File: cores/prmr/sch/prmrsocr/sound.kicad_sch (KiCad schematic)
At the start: 13 parts

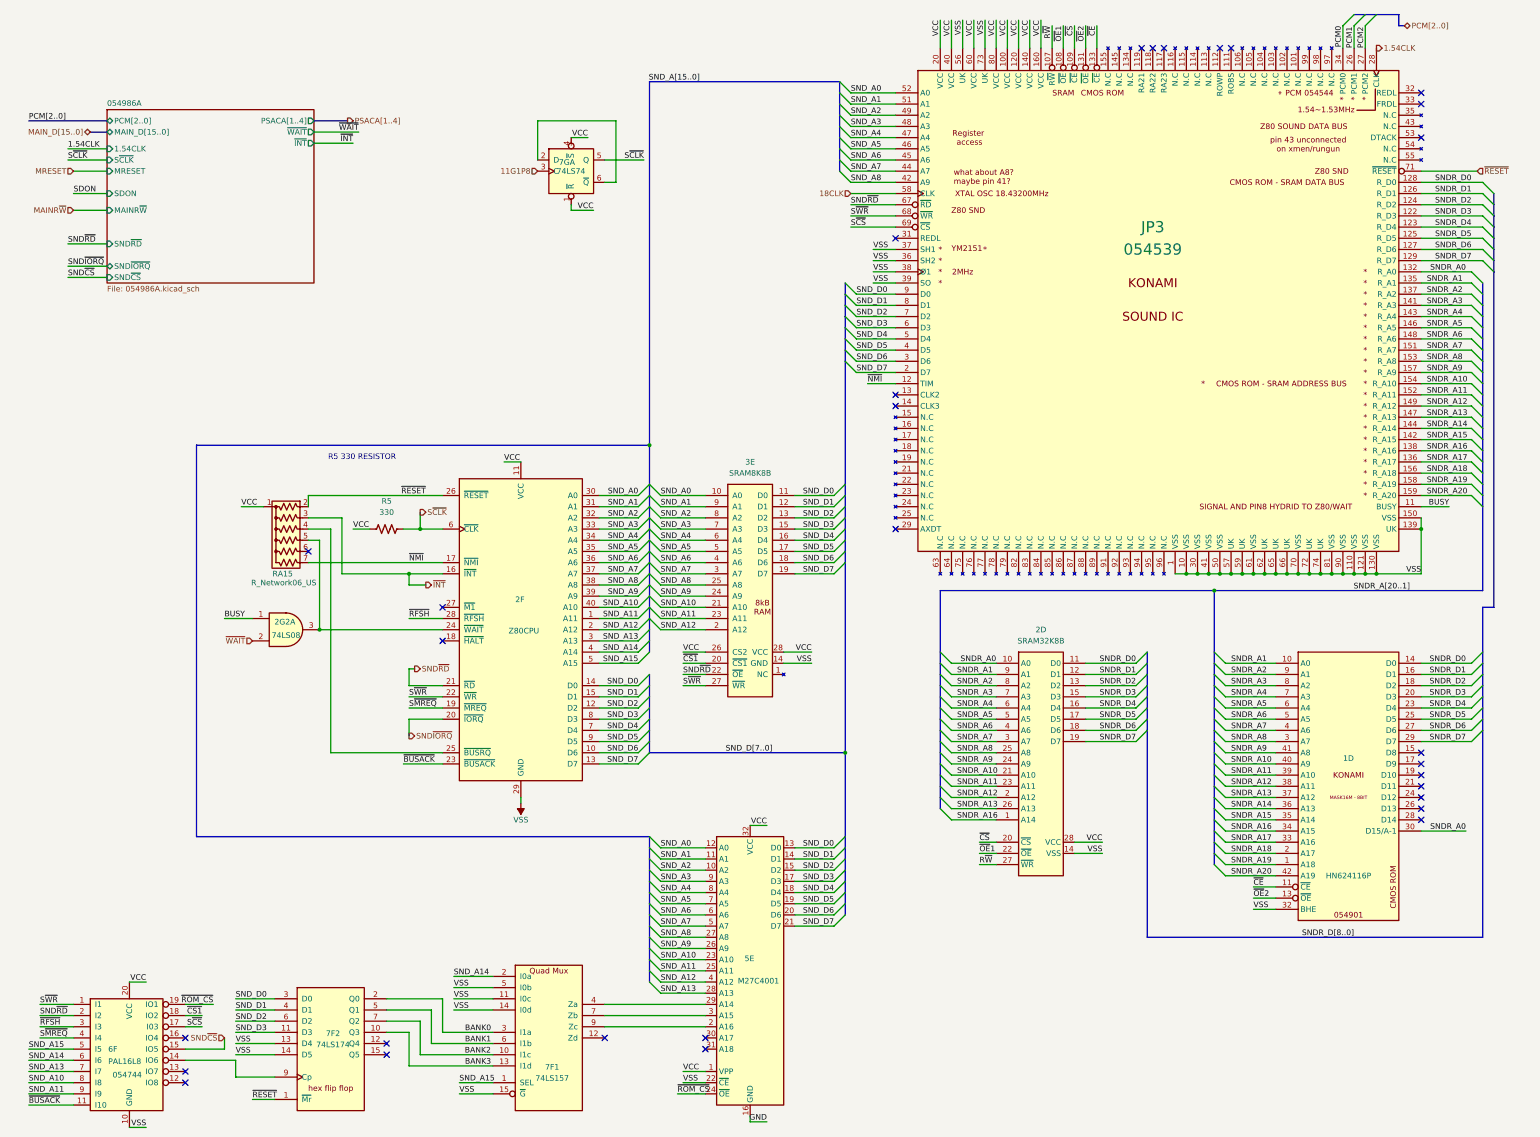
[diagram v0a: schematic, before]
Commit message: edits to prmrsocr schematics. See #1308
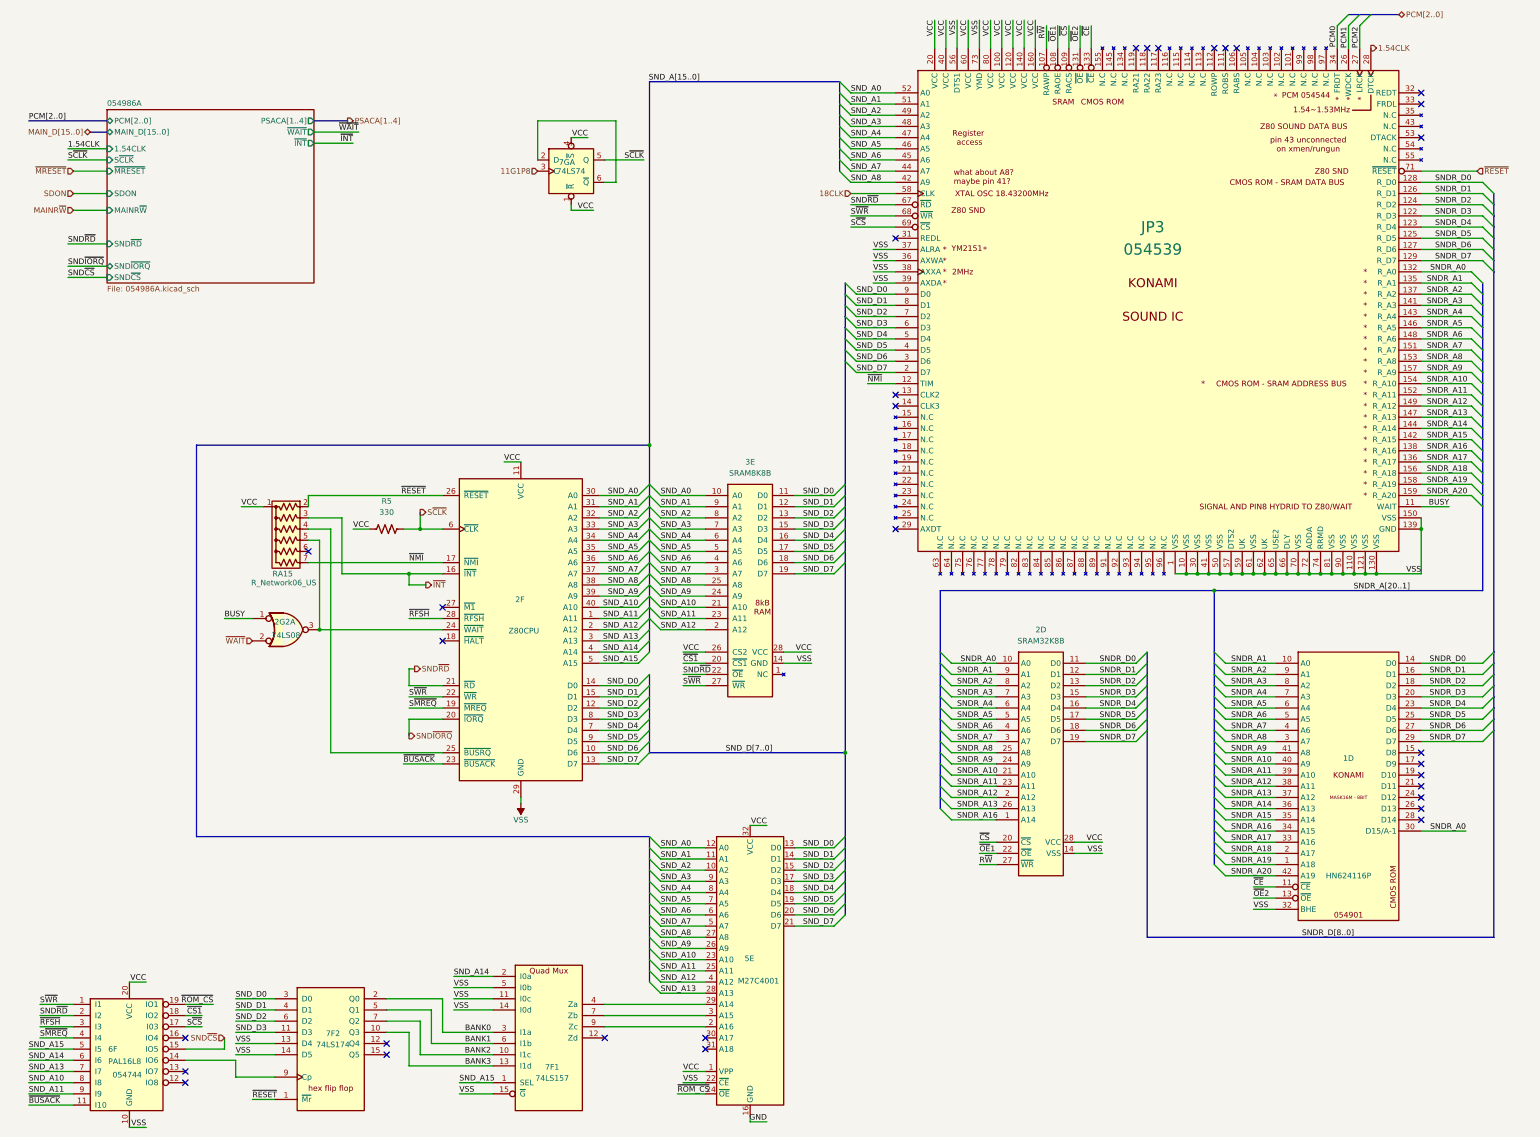
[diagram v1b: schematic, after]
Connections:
- no-connect marks 30 -> 31
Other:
- sheet 054986A ports: added ~{MRESET}; removed MRESET
- note removed: "R5 330 RESISTOR"
